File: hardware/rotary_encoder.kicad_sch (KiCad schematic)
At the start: 9 parts, among them U14 PEC11R-4215F-S0024

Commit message: Removed comments on UART, added some footprints and started fixing rule checks
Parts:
- U14: Manuf. Part # (none) -> PEC11R-4215F-S0024; Part Num PEC11R-4215F-S0024 -> (none); Price/unit $2.4720 -> (none); Supplier Name (none) -> JLCPCB; Supplier Unit Price (none) -> $2.4720
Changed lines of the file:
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@@
+			)
+		)
+		(property "Supplier Name" ""
+			(at 168.91 93.98 0)
+			(effects
+				(font
+					(size 1.27 1.27)
+				)
+				(hide yes)
 			)
 		)
@@
 			)
 		)
+		(property "Supplier Name" ""
+			(at 168.91 102.87 0)
+			(effects
+				(font
+					(size 1.27 1.27)
+				)
+				(hide yes)
+			)
+		)
 		(pin "1"
 		)
@@
 			)
 		)
-		(property "Price/unit" "$2.4720"
+		(property "Package" "Through_Hole"
 			(at 140.97 90.17 0)
 			(effects
@@
 			)
 		)
-		(property "Part Num" "PEC11R-4215F-S0024"
+		(property "Supplier Name" "JLCPCB"
 			(at 140.97 90.17 0)
 			(effects
@@
 			)
 		)
-		(property "Package" "Through_Hole"
+		(property "Manuf. Part #" "PEC11R-4215F-S0024"
+			(at 140.97 90.17 0)
+			(effects
+				(font
+					(size 1.27 1.27)
+				)
+				(hide yes)
+			)
+		)
+		(property "Supplier Unit Price" "$2.4720"
 			(at 140.97 90.17 0)
 			(effects
@@
 			)
 		)
+		(property "Supplier Name" ""
+			(at 114.3 102.87 0)
+			(effects
+				(font
+					(size 1.27 1.27)
+				)
+				(hide yes)
+			)
+		)
 		(pin "1"
 		)
@@
 			)
 		)
+		(property "Supplier Name" ""
+			(at 148.59 67.31 0)
+			(effects
+				(font
+					(size 1.27 1.27)
+				)
+				(hide yes)
+			)
+		)
 		(pin "1"
 		)
@@
 			)
 		)
+		(property "Supplier Name" ""
+			(at 114.3 85.09 0)
+			(effects
+				(font
+					(size 1.27 1.27)
+				)
+				(hide yes)
+			)
+		)
 		(pin "1"
 		)
@@
 			)
 		)
+		(property "Supplier Name" ""
+			(at 114.3 93.98 0)
+			(effects
+				(font
+					(size 1.27 1.27)
+				)
+				(hide yes)
+			)
+		)
 		(pin "1"
 		)
@@
 			)
 		)
+		(property "Supplier Name" ""
+			(at 148.59 76.2 0)
+			(effects
+				(font
+					(size 1.27 1.27)
+				)
+				(hide yes)
+			)
+		)
 		(pin "1"
 		)
@@
 			(at 168.91 85.09 0)
 			(effects
+				(font
+					(size 1.27 1.27)
+				)
+				(hide yes)
+			)
+		)
+		(property "Supplier Name" ""
+			(at 168.91 85.09 0)
+			(effects

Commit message: Added many footprints and populated part of the property tables
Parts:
- C16, C17, C18: footprint (none) -> Capacitor_SMD:C_0805_2012Metric_Pad1.18x1.45mm_HandSolder; Manuf. Name (none) -> Samsung Electro-Mechanics; Manuf. Part # (none) -> CL21B103KBANNNC; Package (none) -> 0805; Supplier Link (none) -> https://jlcpcb.com/partdetail/2062-CL21B103KBANNNC/C1710; Supplier Name (none) -> JLCPCB; Supplier Part # (none) -> C1710; Supplier Unit Price (none) -> $0.0061
- R15, R16, R17, R18, R19: footprint (none) -> Resistor_SMD:R_0805_2012Metric_Pad1.20x1.40mm_HandSolder; Manuf. Name (none) -> UNI-ROYAL(Uniroyal Elec); Manuf. Part # (none) -> 0805W8F1002T5E; Package (none) -> 0805; Supplier Link (none) -> https://jlcpcb.com/partdetail/18102-0805W8F1002T5E/C17414; Supplier Name (none) -> JLCPCB; Supplier Part # (none) -> C17414; Supplier Unit Price (none) -> $0.0017

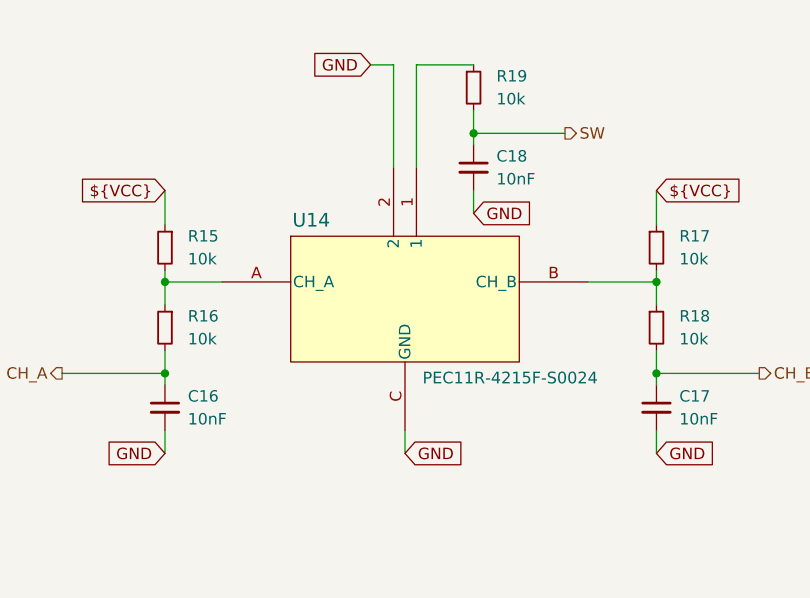
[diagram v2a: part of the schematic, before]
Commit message: Completed the property teble except for the cyristal oscilator
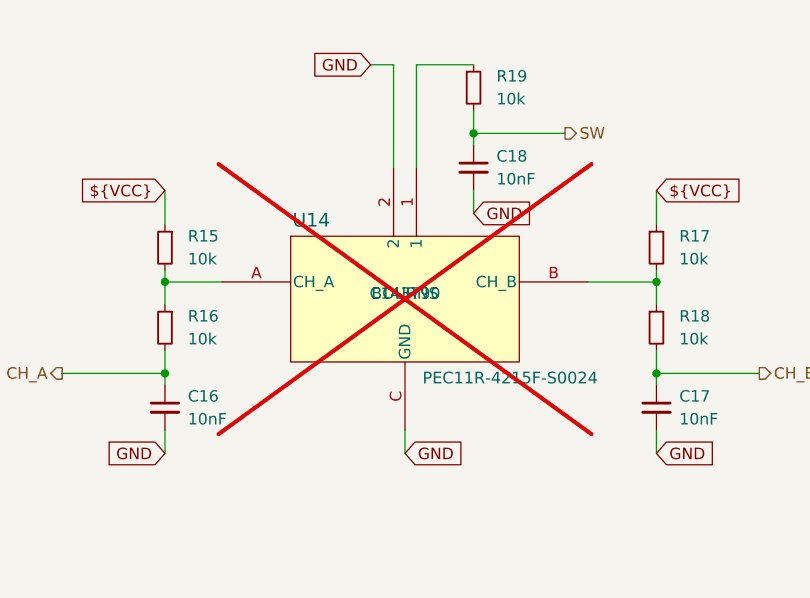
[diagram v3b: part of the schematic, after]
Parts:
- U14: Manuf. Name (none) -> BOURNS; Supplier Part # (none) -> C143790; now not fitted
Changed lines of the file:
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@@
 			)
 		)
-		(property "Description" "Resistor, small symbol"
+		(property "Description" "10k, 0805"
 			(at 168.91 93.98 0)
 			(effects
@@
 		(in_bom yes)
 		(on_board yes)
-		(dnp no)
+		(dnp yes)
 		(property "Reference" "U14"
 			(at 130.556 82.042 0)
@@
 				)
 				(hide yes)
+			)
+		)
+		(property "Manuf. Name" "BOURNS"
+			(at 140.97 90.17 0)
+			(effects
+				(font
+					(size 1.27 1.27)
+				)
+			)
+		)
+		(property "Supplier Part #" "C143790"
+			(at 140.97 90.17 0)
+			(effects
+				(font
+					(size 1.27 1.27)
+				)
 			)
 		)
@@
 			)
 		)
-		(property "Description" "Resistor, small symbol"
+		(property "Description" "10k, 0805"
 			(at 148.59 67.31 0)
 			(effects
@@
 			)
 		)
-		(property "Description" "Resistor, small symbol"
+		(property "Description" "10k, 0805"
 			(at 114.3 85.09 0)
 			(effects
@@
 			)
 		)
-		(property "Description" "Resistor, small symbol"
+		(property "Description" "10k, 0805"
 			(at 114.3 93.98 0)
 			(effects
@@
 			)
 		)
-		(property "Description" "Resistor, small symbol"
+		(property "Description" "10k, 0805"
 			(at 168.91 85.09 0)
 			(effects

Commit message: Made some small changes on the properties of some components while having last weeks meeting and added the fp-info-cache to the gitignore file
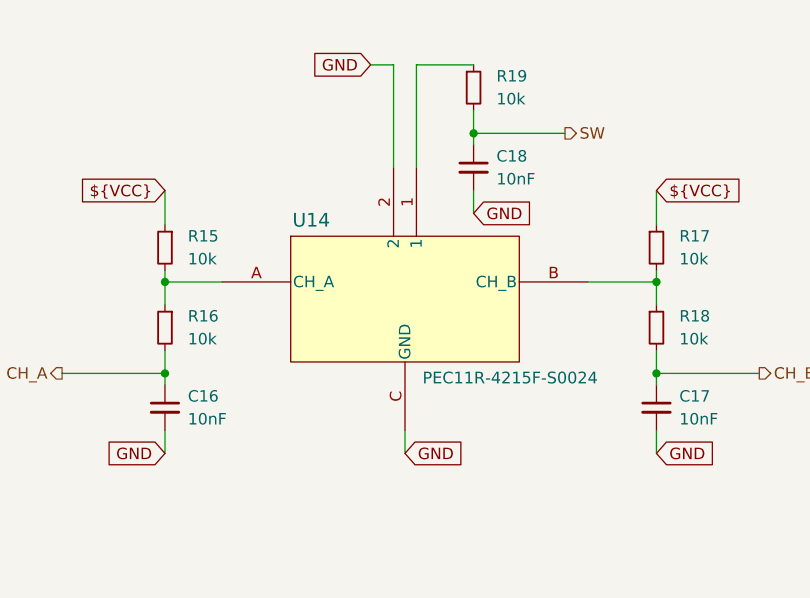
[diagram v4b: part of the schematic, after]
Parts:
- U14: now fitted
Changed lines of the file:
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@@
 		(in_bom yes)
 		(on_board yes)
-		(dnp yes)
+		(dnp no)
 		(property "Reference" "U14"
 			(at 130.556 82.042 0)
@@
 					(size 1.27 1.27)
 				)
+				(hide yes)
 			)
 		)
@@
 					(size 1.27 1.27)
 				)
+				(hide yes)
 			)
 		)

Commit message: Electric Rules Check completed.
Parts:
- removed U14: PEC11R-4215F-S0024, kitchen_timer:PEC11R4215FS0024, symbol kitchen_timer-symbols_lib:PEC11R-4215F-S0024
- added U15: PEC11R-4215F-S0024, kitchen_timer:PEC11R4215FS0024, symbol kitchen_timer-symbols_lib:PEC11R-4215F-S0024
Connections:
- net GND: now also U15.1 (COM), U15.C1 (COMMON)
- net at R17.2, R18.1: now also U15.B1 (CHANNEL_B)
- net at R19.1: now also U15.2 (NO)
- net at R15.2, R16.1: now also U15.A1 (CHANNEL_A)
- no-connect marks 0 -> 2
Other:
- moved on the sheet: C16, C17, C18, R15, R16, R17, R18, R19

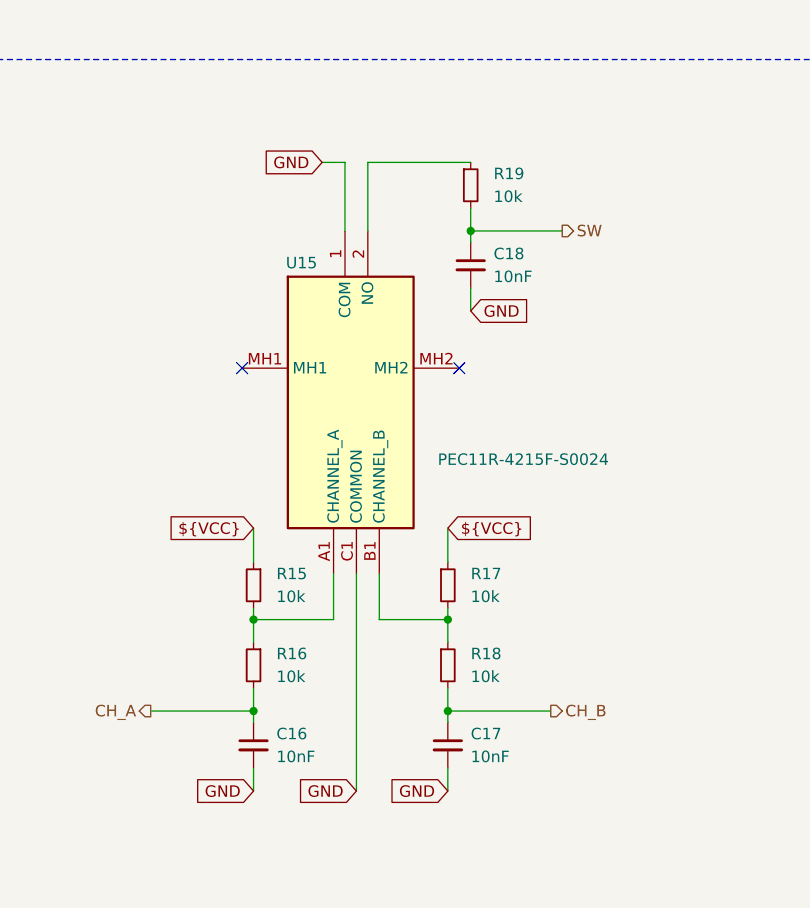
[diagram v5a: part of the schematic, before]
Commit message: Added footprints to mounting holes and selected a part for the test LED.
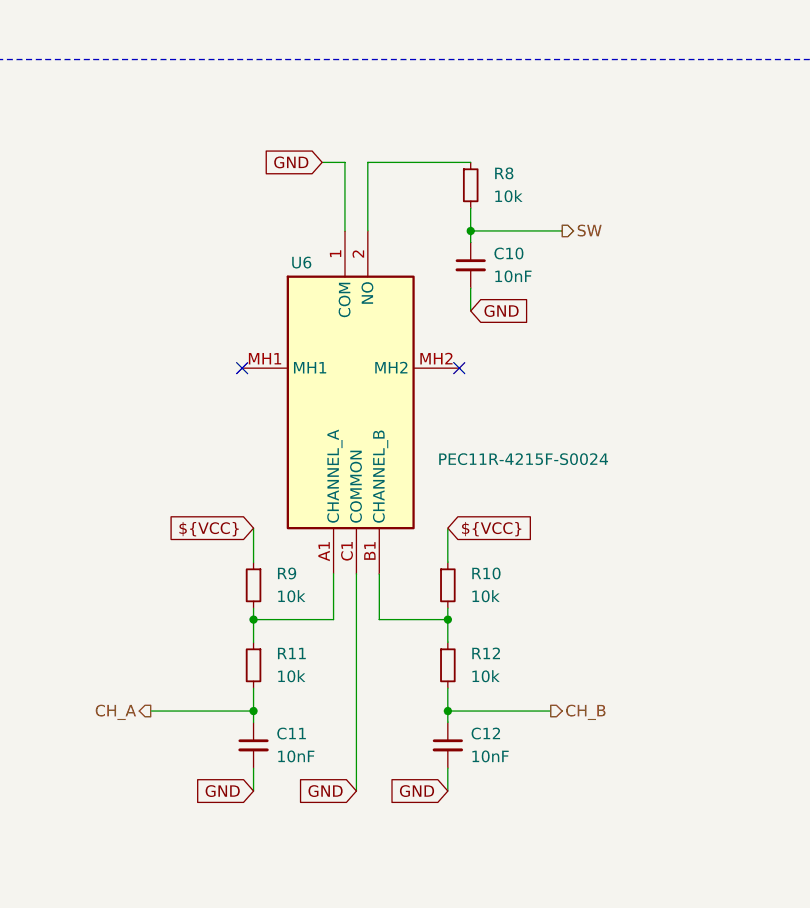
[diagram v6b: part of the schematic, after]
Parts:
- renumbered C18 to C10, C16 to C11, C17 to C12, R17 to R10, R16 to R11, R18 to R12, R19 to R8, R15 to R9, U15 to U6

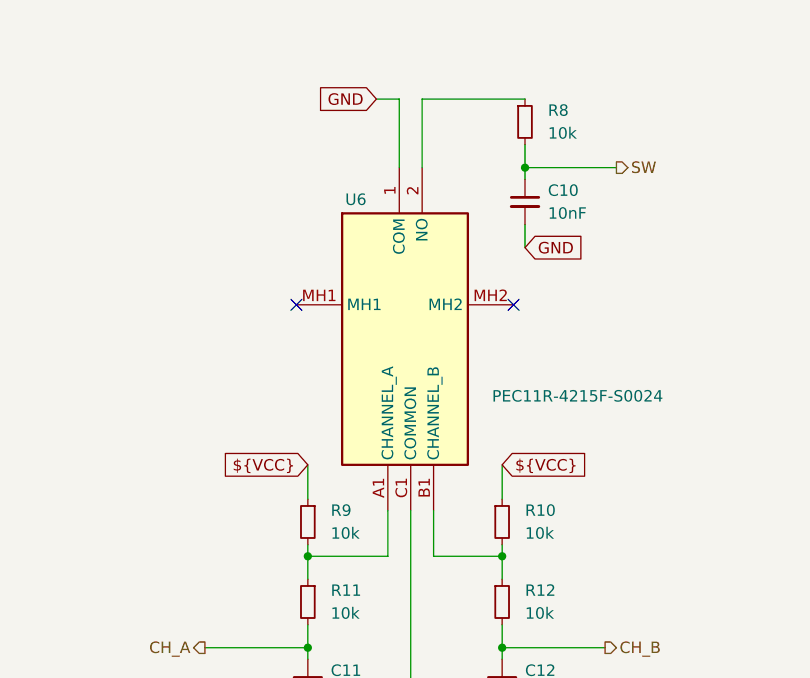
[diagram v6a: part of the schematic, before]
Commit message: Made some items DNP and/or Exclude form Board
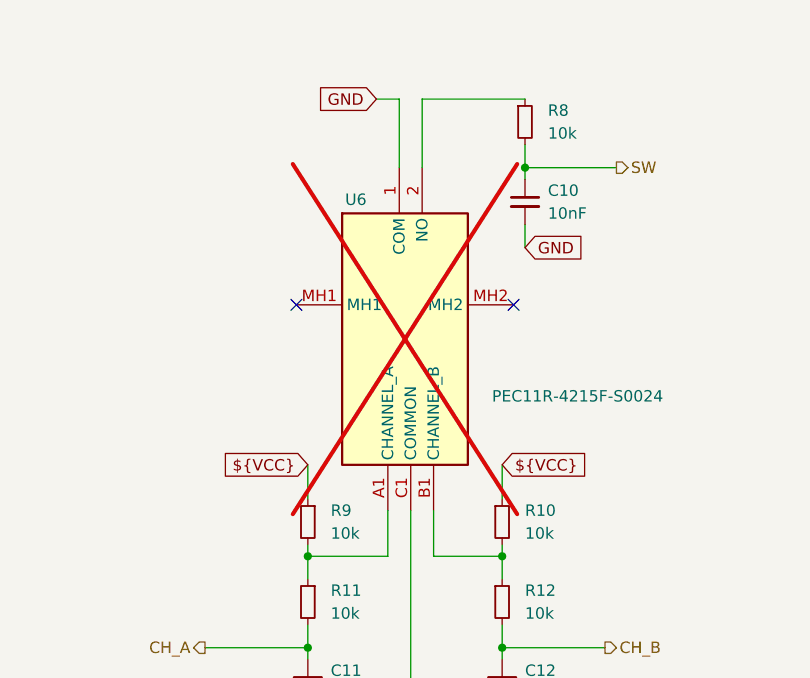
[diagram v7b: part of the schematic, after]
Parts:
- U6: now not fitted
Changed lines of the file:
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@@
 		(in_bom yes)
 		(on_board yes)
-		(dnp no)
+		(dnp yes)
 		(property "Reference" "U6"
 			(at 134.874 79.756 0)

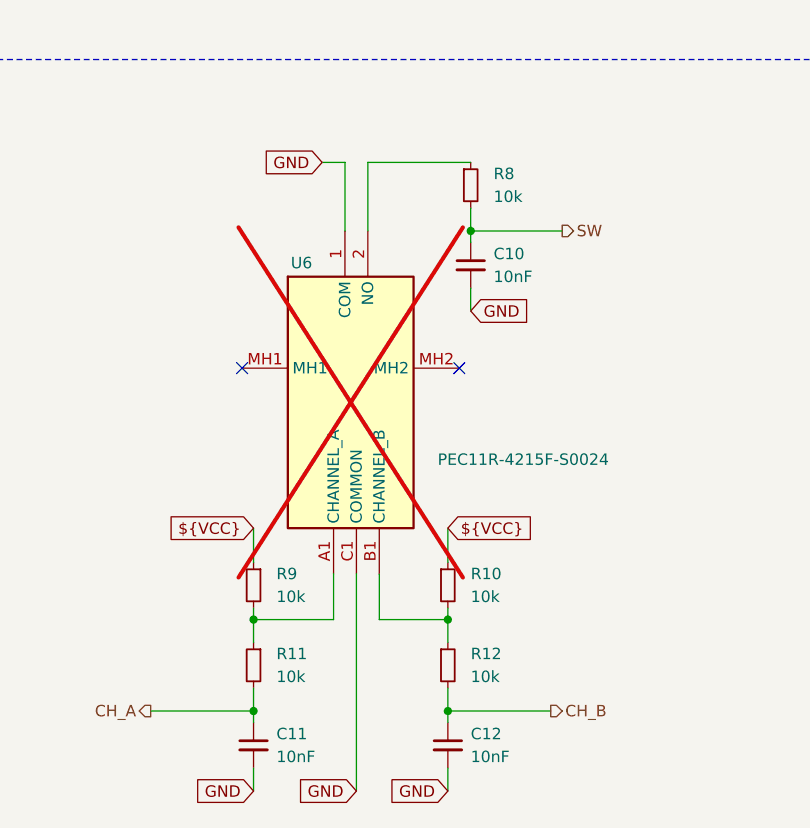
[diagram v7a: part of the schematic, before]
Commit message: Added a pull up resistor to the CS line on the SPI and added two more test LEDs
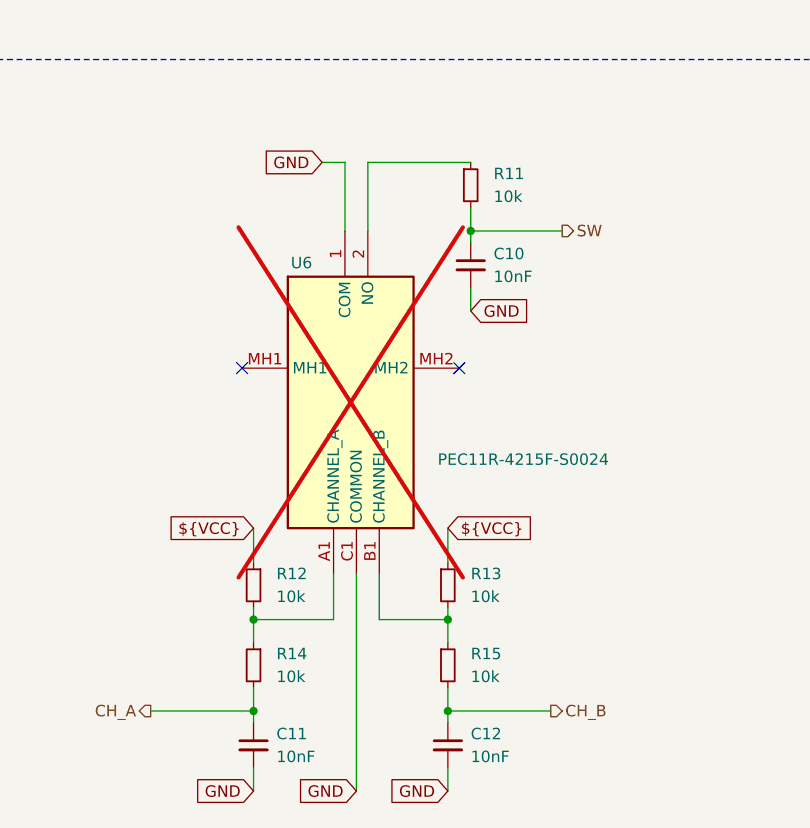
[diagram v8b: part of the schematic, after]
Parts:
- renumbered R8 to R11, R9 to R12, R10 to R13, R11 to R14, R12 to R15
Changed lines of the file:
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@@
 		(dnp no)
 		(fields_autoplaced yes)
-		(property "Reference" "R12"
+		(property "Reference" "R15"
 			(at 153.67 123.1899 0)
 			(effects
@@
 					(size 1.27 1.27)
 				)
+				(hide yes)
 			)
 		)
@@
 					(size 1.27 1.27)
 				)
+				(hide yes)
 			)
 		)
@@
 					(size 1.27 1.27)
 				)
+				(hide yes)
 			)
 		)
@@
 					(size 1.27 1.27)
 				)
+				(hide yes)
 			)
 		)
@@
 			(project "kitchen_timer-hardware"
 				(path "/8963deea-96bc-4401-b671-98fbe9ed9c6a/0bd8e23b-f1a8-43a7-9e7f-c29366033bda"
-					(reference "R12")
+					(reference "R15")
 					(unit 1)
 				)
@@
 					(size 1.27 1.27)
 				)
+				(hide yes)
 			)
 		)
@@
 					(size 1.27 1.27)
 				)
+				(hide yes)
 			)
 		)
@@
 					(size 1.27 1.27)
 				)
+				(hide yes)
 			)
 		)
@@
 					(size 1.27 1.27)
 				)
+				(hide yes)
 			)
 		)
@@
 					(size 1.27 1.27)
 				)
+				(hide yes)
 			)
 		)
@@
 					(size 1.27 1.27)
 				)
+				(hide yes)
 			)
 		)
@@
 					(size 1.27 1.27)
 				)
+				(hide yes)
 			)
 		)
@@
 					(size 1.27 1.27)
 				)
+				(hide yes)
 			)
 		)
@@
 		(dnp no)
 		(fields_autoplaced yes)
-		(property "Reference" "R8"
+		(property "Reference" "R11"
 			(at 156.21 69.8499 0)
 			(effects
@@
 					(size 1.27 1.27)
 				)
+				(hide yes)
 			)
 		)
@@
 					(size 1.27 1.27)
 				)
+				(hide yes)
 			)
 		)
@@
 					(size 1.27 1.27)
 				)
+				(hide yes)
 			)
 		)
@@
 					(size 1.27 1.27)
 				)
+				(hide yes)
 			)
 		)
@@
 			(project "kitchen_timer-hardware"
 				(path "/8963deea-96bc-4401-b671-98fbe9ed9c6a/0bd8e23b-f1a8-43a7-9e7f-c29366033bda"
-					(reference "R8")
+					(reference "R11")
 					(unit 1)
 				)
@@
 		(dnp no)
 		(fields_autoplaced yes)
-		(property "Reference" "R9"
+		(property "Reference" "R12"
 			(at 132.08 114.2999 0)
 			(effects
@@
 					(size 1.27 1.27)
 				)
+				(hide yes)
 			)
 		)
@@
 					(size 1.27 1.27)
 				)
+				(hide yes)
 			)
 		)
@@
 					(size 1.27 1.27)
 				)
+				(hide yes)
 			)
 		)
@@
 					(size 1.27 1.27)
 				)
+				(hide yes)
 			)
 		)
@@
 			(project "kitchen_timer-hardware"
 				(path "/8963deea-96bc-4401-b671-98fbe9ed9c6a/0bd8e23b-f1a8-43a7-9e7f-c29366033bda"
-					(reference "R9")
+					(reference "R12")
 					(unit 1)
 				)
@@
 		(dnp no)
 		(fields_autoplaced yes)
-		(property "Reference" "R11"
+		(property "Reference" "R14"
 			(at 132.08 123.1899 0)
 			(effects
@@
 					(size 1.27 1.27)
 				)
+				(hide yes)
 			)
 		)
@@
 					(size 1.27 1.27)
 				)
+				(hide yes)
 			)
 		)
@@
 					(size 1.27 1.27)
 				)
+				(hide yes)
 			)
 		)
@@
 					(size 1.27 1.27)
 				)
+				(hide yes)
 			)
 		)
@@
 			(project "kitchen_timer-hardware"
 				(path "/8963deea-96bc-4401-b671-98fbe9ed9c6a/0bd8e23b-f1a8-43a7-9e7f-c29366033bda"
-					(reference "R11")
+					(reference "R14")
 					(unit 1)
 				)
@@
 					(size 1.27 1.27)
 				)
+				(hide yes)
 			)
 		)
@@
 					(size 1.27 1.27)
 				)
+				(hide yes)
 			)
 		)
@@
 					(size 1.27 1.27)
 				)
+				(hide yes)
 			)
 		)
@@
 					(size 1.27 1.27)
 				)
+				(hide yes)
 			)
 		)
@@
 					(size 1.27 1.27)
 				)
+				(hide yes)
 			)
 		)
@@
 					(size 1.27 1.27)
 				)
+				(hide yes)
 			)
 		)
@@
 					(size 1.27 1.27)
 				)
+				(hide yes)
 			)
 		)
@@
 					(size 1.27 1.27)
 				)
+				(hide yes)
 			)
 		)
@@
 		(dnp no)
 		(fields_autoplaced yes)
-		(property "Reference" "R10"
+		(property "Reference" "R13"
 			(at 153.67 114.2999 0)
 			(effects
@@
 					(size 1.27 1.27)
 				)
+				(hide yes)
 			)
 		)
@@
 					(size 1.27 1.27)
 				)
+				(hide yes)
 			)
 		)
@@
 					(size 1.27 1.27)
 				)
+				(hide yes)
 			)
 		)
@@
 					(size 1.27 1.27)
 				)
+				(hide yes)
 			)
 		)
@@
 			(project "kitchen_timer-hardware"
 				(path "/8963deea-96bc-4401-b671-98fbe9ed9c6a/0bd8e23b-f1a8-43a7-9e7f-c29366033bda"
-					(reference "R10")
+					(reference "R13")
 					(unit 1)
 				)
